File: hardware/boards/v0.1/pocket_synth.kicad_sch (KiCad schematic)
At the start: 6 parts

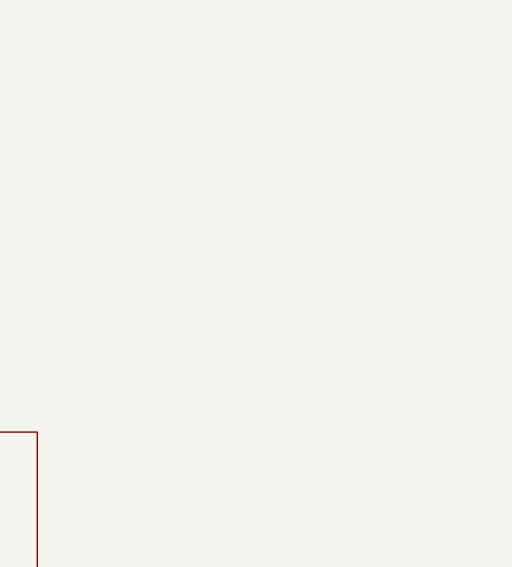
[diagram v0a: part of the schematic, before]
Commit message: feat: various component and layout changes
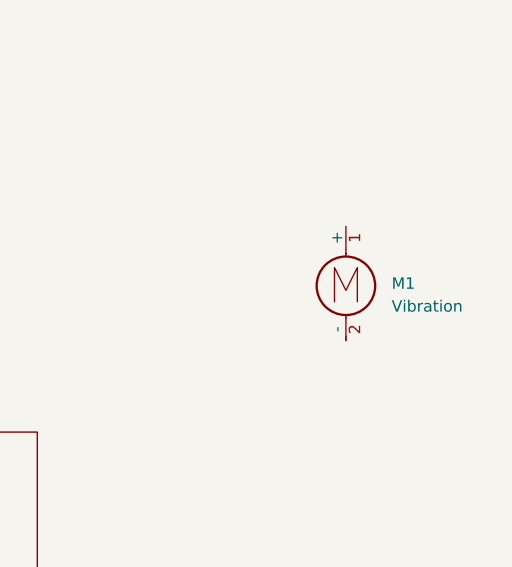
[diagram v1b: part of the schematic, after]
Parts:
- added M1: Vibration, symbol Motor:Motor_DC

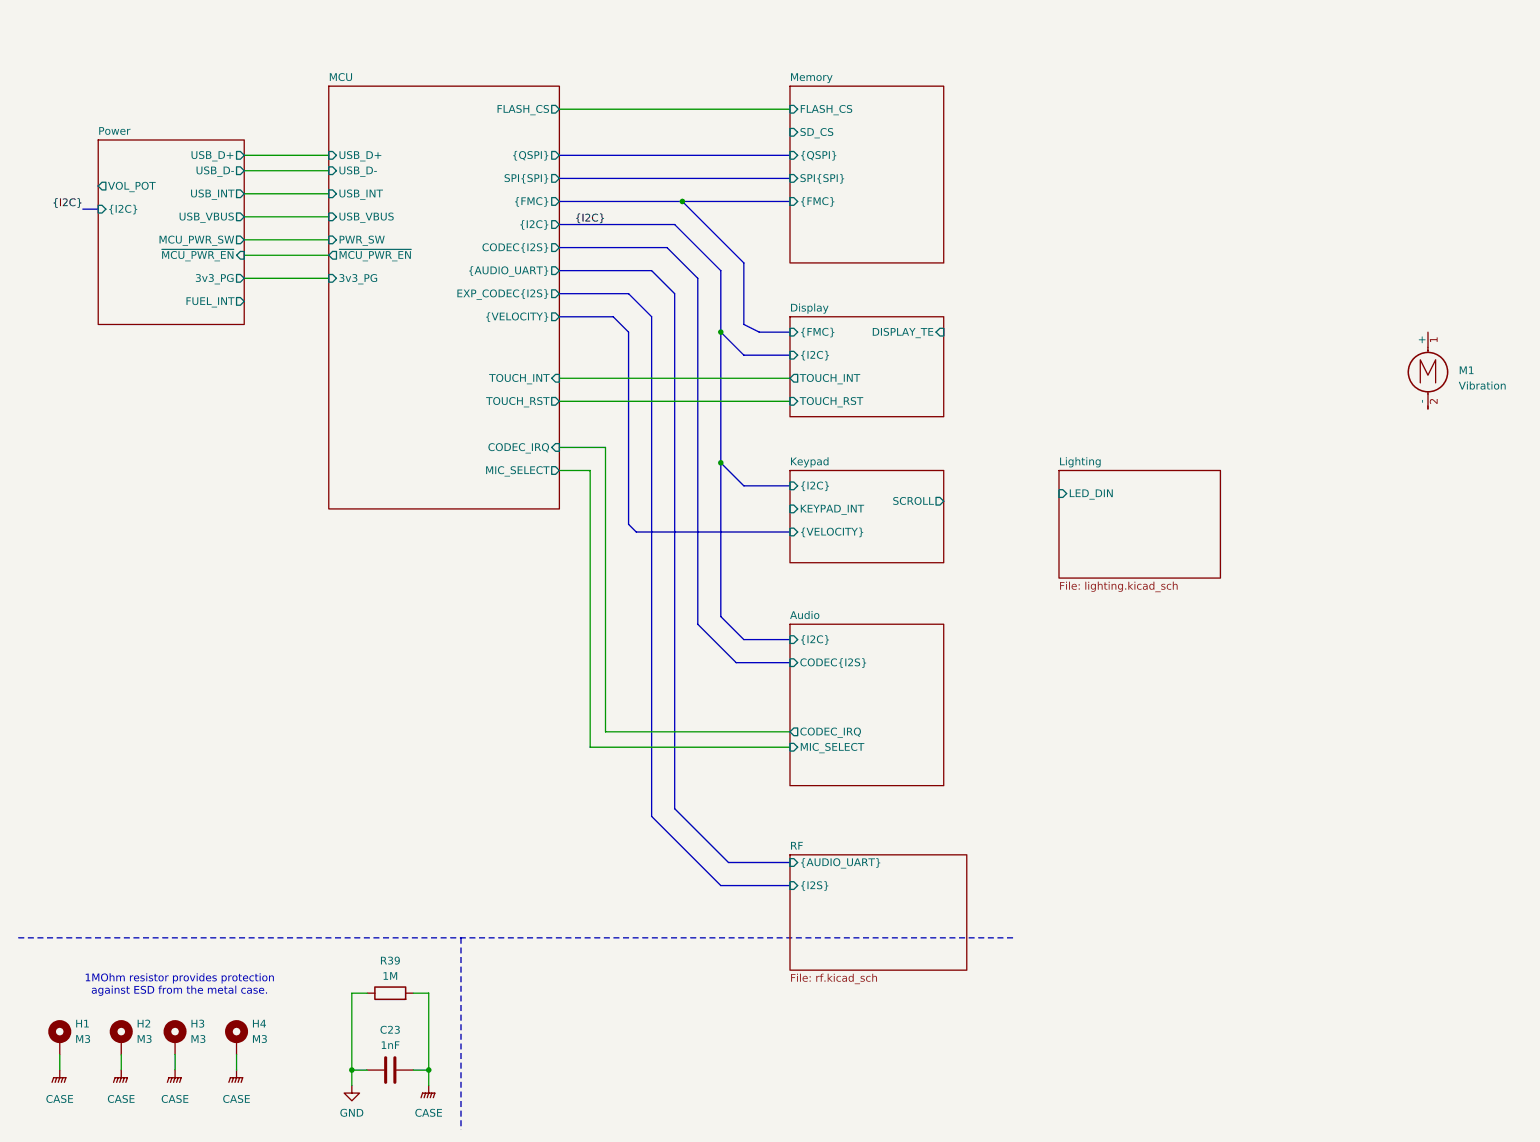
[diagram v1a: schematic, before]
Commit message: feat: add menu buttons and speaker connectors
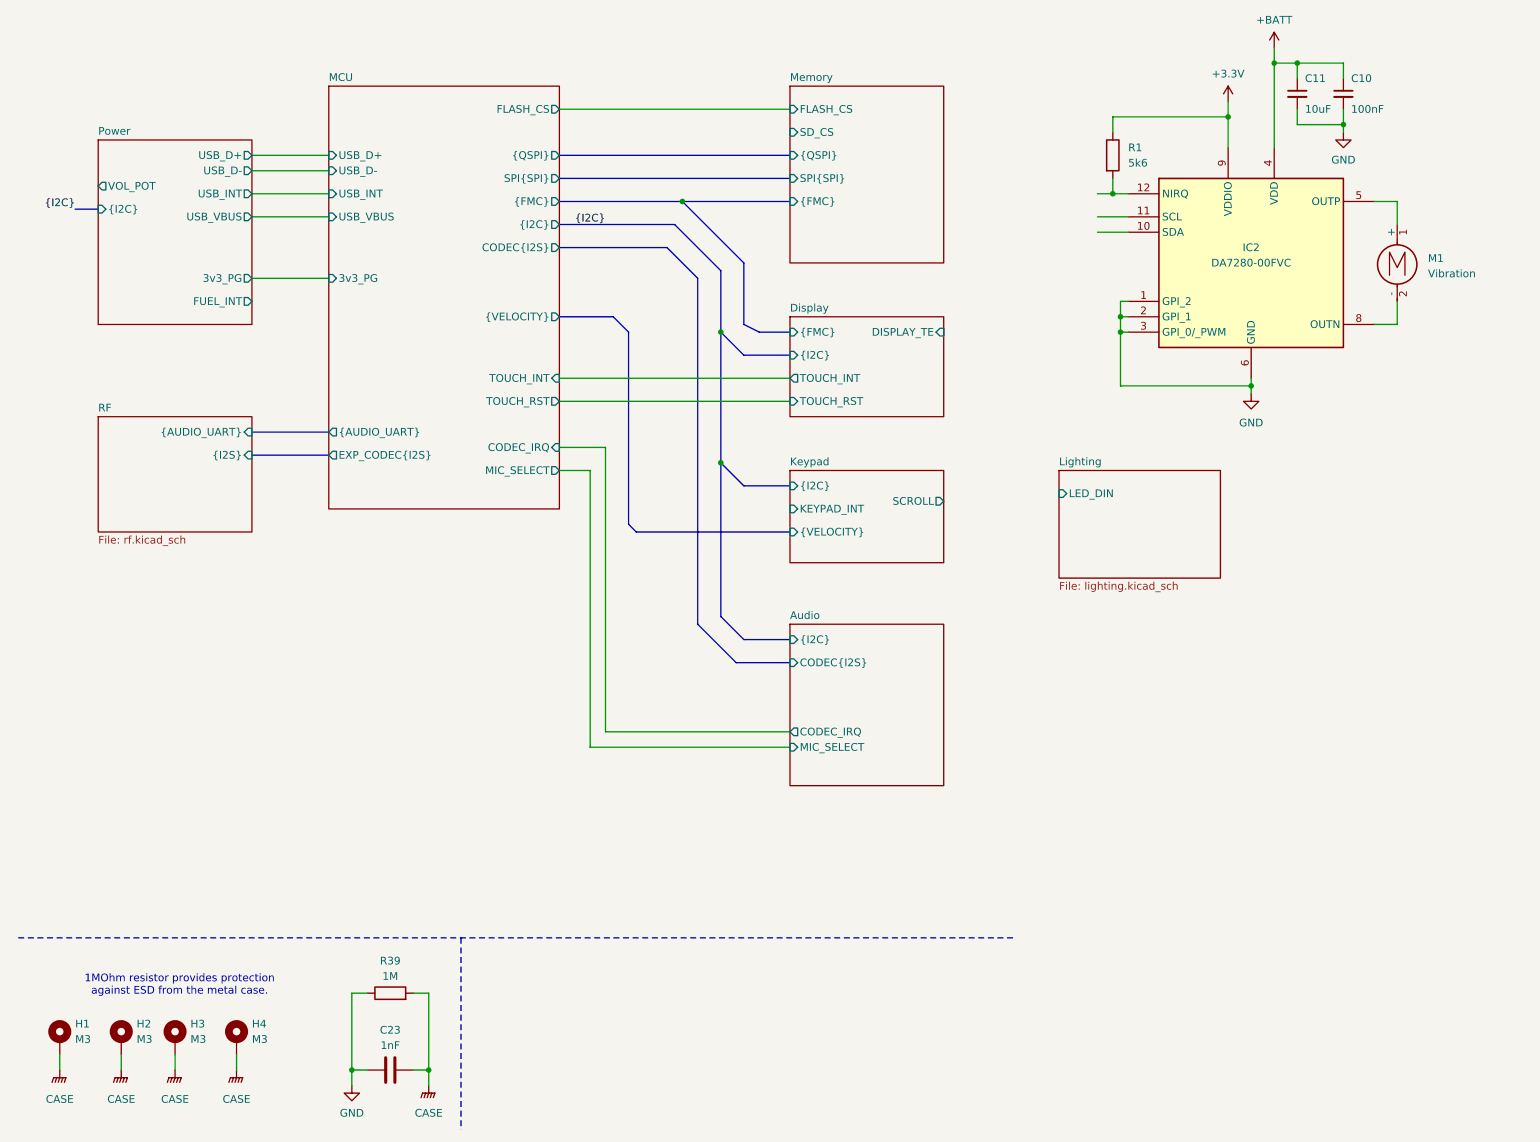
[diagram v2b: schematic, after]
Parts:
- added C10: 100nF, Capacitor_SMD:C_0603_1608Metric, symbol Device:C_Small
- added C11: 10uF, symbol Device:C_Small
- added IC2: DA7280-00FVC, pocket_synth:DA7280-00FVC, symbol pocket_synth:DA7280-00FVC
- added R1: 5k6, symbol Device:R
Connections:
- net GND: now also C10.2, C11.2, IC2.1 (GPI_2), IC2.2 (GPI_1), IC2.3 (GPI_0/_PWM), IC2.6 (GND), IC2.7 (GND_2)
- net at M1.1 (+): now also IC2.5 (OUTP)
- net at M1.2 (-): now also IC2.8 (OUTN)
- new net: IC2.12 (NIRQ), R1.2
- new net +3.3V: IC2.9 (VDDIO), R1.1
- new net +BATT: C10.1, C11.1, IC2.4 (VDD)
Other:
- sheet MCU ports: added none; removed PWR_SW, ~{MCU_PWR_EN}
- sheet Power ports: added none; removed MCU_PWR_SW, ~{MCU_PWR_EN}
- moved on the sheet: M1

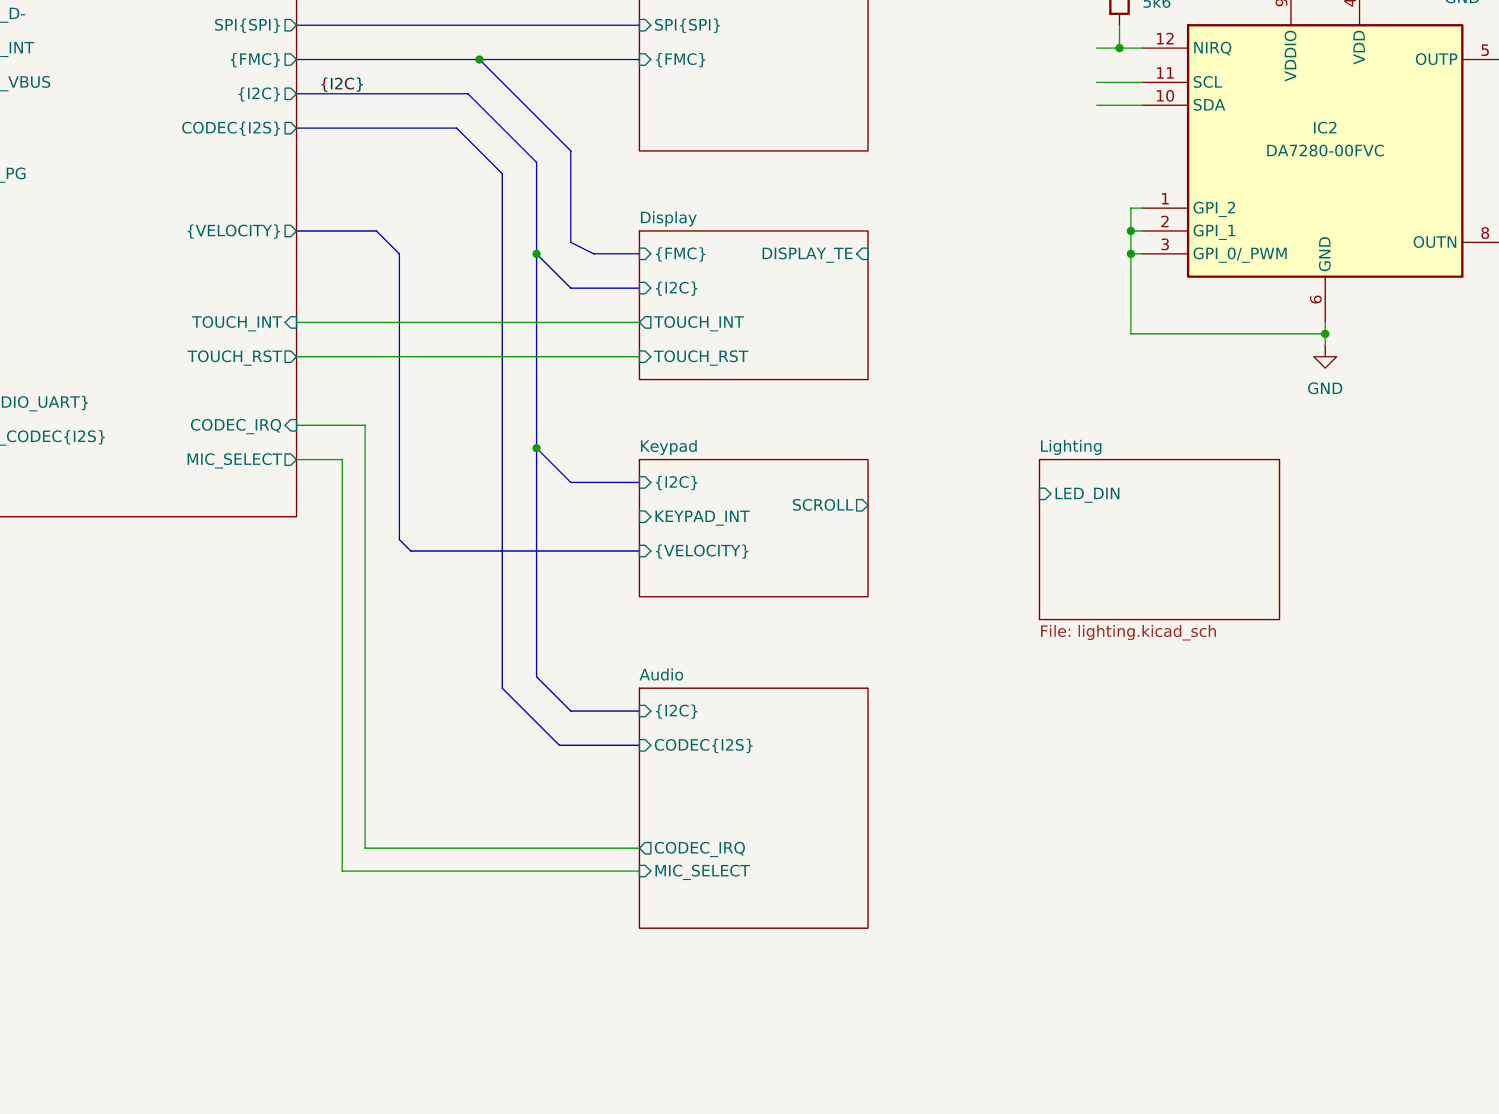
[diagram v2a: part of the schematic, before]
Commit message: feat: start MIDI and CV schematic
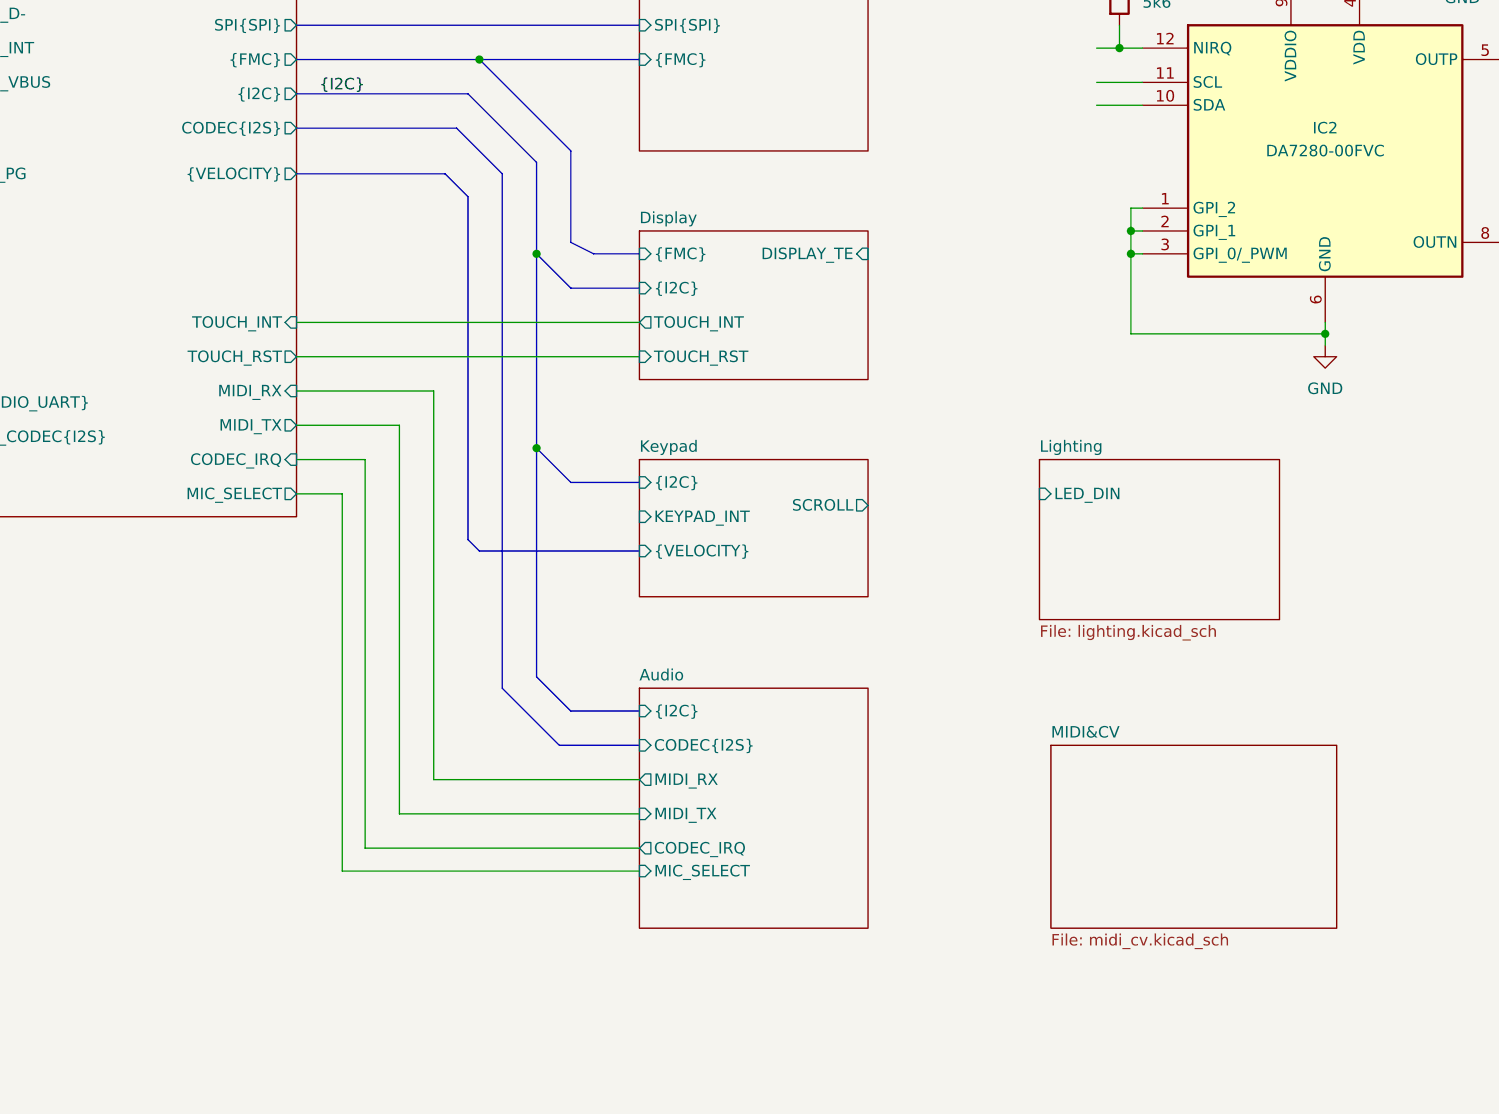
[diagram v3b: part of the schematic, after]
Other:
- added sheet MIDI&CV (midi_cv.kicad_sch)
- sheet Audio ports: added MIDI_RX, MIDI_TX; removed none
- sheet MCU ports: added MIDI_RX, MIDI_TX; removed none
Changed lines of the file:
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@@
 	(bus
 		(pts
-			(xy 113.03 97.79) (xy 114.3 99.06)
+			(xy 120.65 97.79) (xy 121.92 99.06)
 		)
 		(stroke
@@
 	(wire
 		(pts
+			(xy 113.03 128.27) (xy 139.7 128.27)
+		)
+		(stroke
+			(width 0)
+			(type default)
+		)
+	)
+	(wire
+		(pts
 			(xy 50.8 39.37) (xy 63.5 39.37)
 		)
@@
 	(wire
 		(pts
-			(xy 109.22 85.09) (xy 109.22 132.08)
+			(xy 109.22 88.9) (xy 109.22 132.08)
 		)
 		(stroke
@@
 	(wire
 		(pts
-			(xy 101.6 88.9) (xy 106.68 88.9)
+			(xy 101.6 92.71) (xy 106.68 92.71)
 		)
 		(stroke
@@
 		)
 	)
+	(bus
+		(pts
+			(xy 101.6 57.15) (xy 118.11 57.15)
+		)
+		(stroke
+			(width 0)
+			(type default)
+		)
+	)
 	(wire
 		(pts
@@
 	(wire
 		(pts
-			(xy 101.6 85.09) (xy 109.22 85.09)
+			(xy 101.6 88.9) (xy 109.22 88.9)
 		)
 		(stroke
@@
 	(wire
 		(pts
+			(xy 116.84 81.28) (xy 116.84 124.46)
+		)
+		(stroke
+			(width 0)
+			(type default)
+		)
+	)
+	(wire
+		(pts
 			(xy 193.04 30.48) (xy 193.04 33.02)
 		)
@@
 	(bus
 		(pts
-			(xy 113.03 66.04) (xy 113.03 97.79)
+			(xy 120.65 59.69) (xy 120.65 97.79)
 		)
 		(stroke
@@
 	(wire
 		(pts
+			(xy 101.6 81.28) (xy 116.84 81.28)
+		)
+		(stroke
+			(width 0)
+			(type default)
+		)
+	)
+	(wire
+		(pts
 			(xy 50.8 36.83) (xy 63.5 36.83)
 		)
@@
 	(wire
 		(pts
-			(xy 106.68 88.9) (xy 106.68 134.62)
+			(xy 106.68 92.71) (xy 106.68 134.62)
 		)
 		(stroke
@@
 	(bus
 		(pts
-			(xy 101.6 63.5) (xy 110.49 63.5)
+			(xy 132.08 54.61) (xy 132.08 64.77)
 		)
 		(stroke
@@
 	(bus
 		(pts
-			(xy 132.08 54.61) (xy 132.08 64.77)
+			(xy 124.46 57.15) (xy 124.46 114.3)
 		)
 		(stroke
@@
 	(bus
 		(pts
-			(xy 124.46 57.15) (xy 124.46 114.3)
+			(xy 50.8 86.36) (xy 63.5 86.36)
 		)
 		(stroke
@@
 		)
 	)
-	(bus
+	(wire
 		(pts
-			(xy 50.8 86.36) (xy 63.5 86.36)
+			(xy 113.03 85.09) (xy 113.03 128.27)
 		)
 		(stroke
@@
 	(wire
 		(pts
+			(xy 116.84 124.46) (xy 139.7 124.46)
+		)
+		(stroke
+			(width 0)
+			(type default)
+		)
+	)
+	(wire
+		(pts
 			(xy 80.01 187.96) (xy 80.01 190.5)
 		)
@@
 	(wire
 		(pts
+			(xy 101.6 85.09) (xy 113.03 85.09)
+		)
+		(stroke
+			(width 0)
+			(type default)
+		)
+	)
+	(wire
+		(pts
 			(xy 194.31 63.5) (xy 194.31 66.04)
 		)
@@
 	(bus
 		(pts
-			(xy 114.3 99.06) (xy 139.7 99.06)
+			(xy 121.92 99.06) (xy 139.7 99.06)
 		)
 		(stroke
@@
 	(bus
 		(pts
-			(xy 110.49 63.5) (xy 113.03 66.04)
+			(xy 118.11 57.15) (xy 120.65 59.69)
 		)
 		(stroke
@@
 		)
 		(pin "CODEC_IRQ" input
-			(at 101.6 85.09 0)
+			(at 101.6 88.9 0)
 			(effects
 				(font
@@
 		)
 		(pin "MIC_SELECT" output
-			(at 101.6 88.9 0)
+			(at 101.6 92.71 0)
 			(effects
 				(font
@@
 		)
 		(pin "{VELOCITY}" output
-			(at 101.6 63.5 0)
+			(at 101.6 57.15 0)
+			(effects
+				(font
+					(size 1.27 1.27)
+				)
+				(justify right)
+			)
+		)
+		(pin "MIDI_RX" input
+			(at 101.6 81.28 0)
+			(effects
+				(font
+					(size 1.27 1.27)
+				)
+				(justify right)
+			)
+		)
+		(pin "MIDI_TX" output
+			(at 101.6 85.09 0)
 			(effects
 				(font
@@
 	)
 	(sheet
+		(at 185.42 120.65)
+		(size 31.75 20.32)
+		(exclude_from_sim no)
+		(in_bom yes)
+		(on_board yes)
+		(dnp no)
+		(fields_autoplaced yes)
+		(stroke
+			(width 0.1524)
+			(type solid)
+		)
+		(fill
+			(color 0 0 0 0.0000)
+		)
+		(property "Sheetname" "MIDI&CV"
+			(at 185.42 119.9384 0)
+			(effects
+				(font
+					(size 1.27 1.27)
+				)
+				(justify left bottom)
+			)
+		)
+		(property "Sheetfile" "midi_cv.kicad_sch"
+			(at 185.42 141.5546 0)
+			(effects
+				(font
+					(size 1.27 1.27)
+				)
+				(justify left top)
+			)
+		)
+		(instances
+			(project "pocket_synth"
+				(path "/485383b8-00f4-4405-b270-de249939cff4"
+					(page "10")
+				)
+			)
+		)
+	)
+	(sheet
 		(at 25.4 34.29)
 		(size 25.4 30.48)
@@
 			(effects
 				(font
+					(size 1.27 1.27)
+				)
+				(justify left)
+			)
+		)
+		(pin "MIDI_RX" output
+			(at 139.7 124.46 180)
+			(effects
+				(font
+					(size 1.27 1.27)
+				)
+				(justify left)
+			)
+		)
+		(pin "MIDI_TX" input
+			(at 139.7 128.27 180)
+			(effects
+				(font

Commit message: feat: various schematic organization
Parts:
- removed C10: 100nF, Capacitor_SMD:C_0603_1608Metric, symbol Device:C_Small
- removed C11: 10uF, symbol Device:C_Small
- removed IC2: DA7280-00FVC, pocket_synth:DA7280-00FVC, symbol pocket_synth:DA7280-00FVC
- removed M1: Vibration, symbol Motor:Motor_DC
- removed R1: 5k6, symbol Device:R
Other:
- added sheet Peripherals (peripherals.kicad_sch)
- sheet Keypad ports: added none; removed SCROLL
- sheet MIDI&CV ports: added MIDI_RX, MIDI_THRU_EN, MIDI_TX; removed none
- sheet Power ports: added none; removed VOL_POT
